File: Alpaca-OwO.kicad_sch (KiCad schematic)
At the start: 43 parts, among them J1 SWD, J2 PS360 ST1, J3 PS360 ST2, J4 Stick, J5 USB_B, J6 Pwny Pr0t, J7 I2C Quick connect, Q1 CJL3415, SW1 Reset, SW2 I2C Pullup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

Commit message: Import LCSC parts info for all components except pin headers.
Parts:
- C1, C2: value 10uF -> (none); footprint Capacitor_Tantalum_SMD:CP_EIA-3216-18_Kemet-A -> (none)
- C10, C12, C13, C14, C15, C16, C6, C7, C8, C9: value 100nF -> (none); footprint Capacitor_SMD:C_0603_1608Metric -> (none); JLC (none) -> 0603; LCSC (none) -> C1591
- C11, C5: value 1uF -> (none); footprint Capacitor_SMD:C_0603_1608Metric -> (none); JLC (none) -> 0603; LCSC (none) -> C1592
- C3, C4: value 30pF -> (none); footprint Capacitor_SMD:C_0603_1608Metric -> (none); JLC (none) -> 0603; LCSC (none) -> C713507
- F1: value 500mA -> (none); footprint Fuse:Fuse_1210_3225Metric -> (none)
- H1, H2, H3, H4: value M3 -> (none); footprint MountingHole:MountingHole_3.2mm_M3_ISO7380 -> (none)
- J1: value SWD -> (none); footprint Connector_PinHeader_2.54mm:PinHeader_1x05_P2.54mm_Vertical -> (none); JLC (none) -> Plugin,P=2.54mm
- J2: value PS360 ST1 -> (none); footprint Connector_Phoenix_MC:PhoenixContact_MC_1,5_10-G-3.5_1x10_P3.50mm_Horizontal -> (none); Comments (none) -> Use equivalent Chinese connector for JLCPCBA. Mate with Min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; JLC (none) -> P=3.5mm; LCSC (none) -> C880580
- J3: value PS360 ST2 -> (none); footprint Connector_Phoenix_MC:PhoenixContact_MC_1,5_10-G-3.5_1x10_P3.50mm_Horizontal -> (none); Comments (none) -> Use equivalent Chinese connector for JLCPCBA. Mate with Min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; JLC (none) -> P=3.5mm; LCSC (none) -> C880580
- J4: value Stick -> (none); footprint Connector_PinHeader_2.54mm:PinHeader_1x08_P2.54mm_Vertical -> (none); JLC (none) -> Plugin,P=2.54mm
- J5: value USB_B -> (none); footprint Connector_USB:USB_B_OST_USB-B1HSxx_Horizontal -> (none); JLC (none) -> Plugin; LCSC (none) -> C46392
- J6: value Pwny Pr0t -> (none); footprint Connector_PinHeader_2.54mm:PinHeader_2x08_P2.54mm_Vertical -> (none); JLC (none) -> Plugin,P=2.54mm
- J7: value I2C Quick connect -> (none); footprint Connector_JST:JST_SH_SM04B-SRSS-TB_1x04-1MP_P1.00mm_Horizontal -> (none); JLC (none) -> -; LCSC (none) -> C160404
- Q1: value CJL3415 -> (none); footprint Package_TO_SOT_SMD:SOT-23-6 -> (none)
- R1: value 10k -> (none); footprint Resistor_SMD:R_0603_1608Metric -> (none); JLC (none) -> 0603; LCSC (none) -> C98220
- R2, R5, R6, R7: value 1k -> (none); footprint Resistor_SMD:R_0603_1608Metric -> (none); JLC (none) -> 0603; LCSC (none) -> C116692
- R3, R4: value 27 -> (none); footprint Resistor_SMD:R_0603_1608Metric -> (none); JLC (none) -> 0603; LCSC (none) -> C137753
- SW1: value Reset -> (none); footprint Button_Switch_THT:SW_PUSH_6mm -> (none); JLC (none) -> Plugin; LCSC (none) -> C393938
- SW2: value I2C Pullup -> (none); footprint Button_Switch_THT:SW_DIP_SPSTx02_Slide_9.78x7.26mm_W7.62mm_P2.54mm -> (none); JLC (none) -> Plugin; LCSC (none) -> C319062
- SW3: value BootSel -> (none); footprint Button_Switch_THT:SW_PUSH_6mm -> (none); JLC (none) -> Plugin; LCSC (none) -> C393938
- U1: value AMS1117-3.3 -> (none); footprint Package_TO_SOT_SMD:SOT-223-3_TabPin2 -> (none); JLC (none) -> SOT-223; LCSC (none) -> C6186
- U2: value RP2040 -> (none); footprint private:QFN-56-1EP_7x7mm_P0.4mm_EP3.2x3.2mm_ThermalVias -> (none); JLC (none) -> QFN-56(7x7); LCSC (none) -> C2040
- U3: value W25Q32JVSS -> (none); footprint Package_SO:SOIC-8_5.23x5.23mm_P1.27mm -> (none); JLC (none) -> SOIC-8_208mil; LCSC (none) -> C82344
- Y1: value 12MHz -> (none); footprint Crystal:Crystal_HC49-4H_Vertical -> (none)

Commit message: Set screw holes as do not include
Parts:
- C1, C2: value (none) -> 10uF; footprint (none) -> Capacitor_Tantalum_SMD:CP_EIA-3216-18_Kemet-A
- C10, C12, C13, C14, C15, C16, C6, C7, C8, C9: value (none) -> 100nF; footprint (none) -> Capacitor_SMD:C_0603_1608Metric
- C11, C5: value (none) -> 1uF; footprint (none) -> Capacitor_SMD:C_0603_1608Metric
- C3, C4: value (none) -> 30pF; footprint (none) -> Capacitor_SMD:C_0603_1608Metric
- F1: value (none) -> 500mA; footprint (none) -> Fuse:Fuse_1210_3225Metric
- H1, H2, H3, H4: now left out of the parts list
- J1: value (none) -> SWD; footprint (none) -> Connector_PinHeader_2.54mm:PinHeader_1x05_P2.54mm_Vertical
- J2: value (none) -> PS360 ST1; footprint (none) -> Connector_Phoenix_MC:PhoenixContact_MC_1,5_10-G-3.5_1x10_P3.50mm_Horizontal
- J3: value (none) -> PS360 ST2; footprint (none) -> Connector_Phoenix_MC:PhoenixContact_MC_1,5_10-G-3.5_1x10_P3.50mm_Horizontal
- J4: value (none) -> Stick; footprint (none) -> Connector_PinHeader_2.54mm:PinHeader_1x08_P2.54mm_Vertical
- J5: value (none) -> USB_B; footprint (none) -> Connector_USB:USB_B_OST_USB-B1HSxx_Horizontal
- J6: value (none) -> Pwny Pr0t; footprint (none) -> Connector_PinHeader_2.54mm:PinHeader_2x08_P2.54mm_Vertical
- J7: value (none) -> I2C Quick connect; footprint (none) -> Connector_JST:JST_SH_SM04B-SRSS-TB_1x04-1MP_P1.00mm_Horizontal
- Q1: value (none) -> CJL3415; footprint (none) -> Package_TO_SOT_SMD:SOT-23-6
- R1: value (none) -> 10k; footprint (none) -> Resistor_SMD:R_0603_1608Metric
- R2, R5, R6, R7: value (none) -> 1k; footprint (none) -> Resistor_SMD:R_0603_1608Metric
- R3, R4: value (none) -> 27; footprint (none) -> Resistor_SMD:R_0603_1608Metric
- SW1: value (none) -> Reset; footprint (none) -> Button_Switch_THT:SW_PUSH_6mm
- SW2: value (none) -> I2C Pullup; footprint (none) -> Button_Switch_THT:SW_DIP_SPSTx02_Slide_9.78x7.26mm_W7.62mm_P2.54mm
- SW3: value (none) -> BootSel; footprint (none) -> Button_Switch_THT:SW_PUSH_6mm
- U1: value (none) -> AMS1117-3.3; footprint (none) -> Package_TO_SOT_SMD:SOT-223-3_TabPin2
- U2: value (none) -> RP2040; footprint (none) -> private:QFN-56-1EP_7x7mm_P0.4mm_EP3.2x3.2mm_ThermalVias
- U3: value (none) -> W25Q32JVSS; footprint (none) -> Package_SO:SOIC-8_5.23x5.23mm_P1.27mm
- Y1: value (none) -> 12MHz; footprint (none) -> Crystal:Crystal_HC49-4H_Vertical

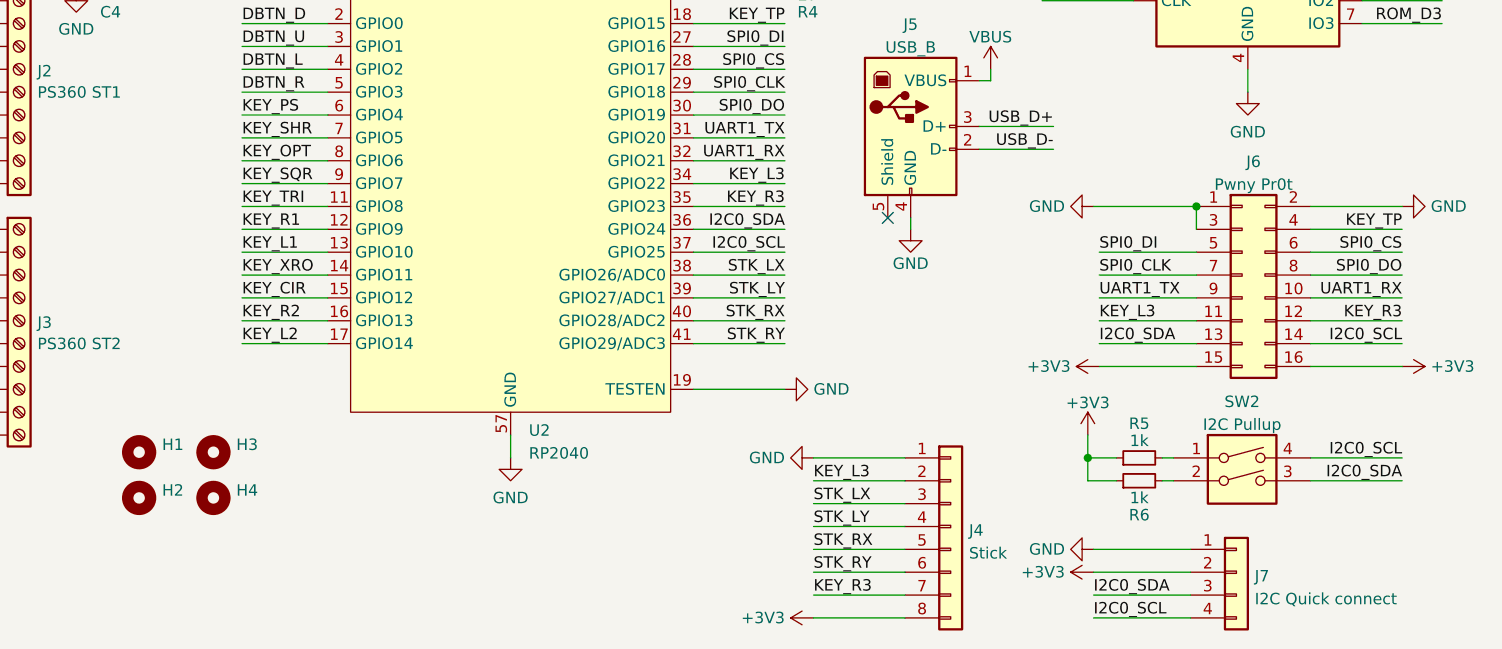
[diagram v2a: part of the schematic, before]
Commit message: v1.11
Fixed an issue where the analog stick port does not follow the Brook pinout.

No PCB routing was changed but the pin assignment for stick axis and L3/R3 buttons are now mirrored. Refer to README for the new pinout.
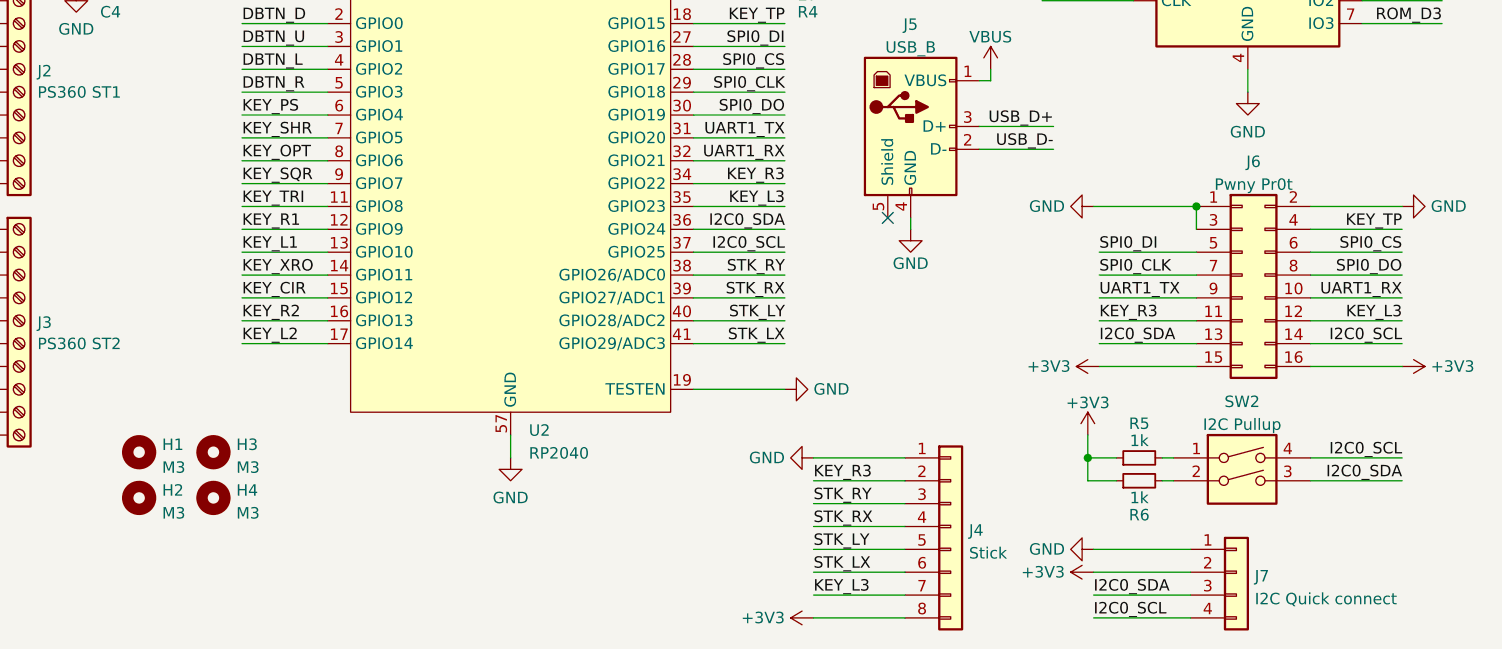
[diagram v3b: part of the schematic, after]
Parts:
- H1, H2, H3, H4: value (none) -> M3; footprint (none) -> MountingHole:MountingHole_3.2mm_M3_ISO7380
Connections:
- net KEY_L3: now also J4.7 (Pin_7), J6.12 (Pin_12), U2.35 (GPIO23); no longer J4.2 (Pin_2), J6.11 (Pin_11), U2.34 (GPIO22)
- net KEY_R3: now also J4.2 (Pin_2), J6.11 (Pin_11), U2.34 (GPIO22); no longer J4.7 (Pin_7), J6.12 (Pin_12), U2.35 (GPIO23)
- net STK_LX: now also J4.6 (Pin_6), U2.41 (GPIO29/ADC3); no longer J4.3 (Pin_3), U2.38 (GPIO26/ADC0)
- net STK_LY: now also J4.5 (Pin_5), U2.40 (GPIO28/ADC2); no longer J4.4 (Pin_4), U2.39 (GPIO27/ADC1)
- net STK_RX: now also J4.4 (Pin_4), U2.39 (GPIO27/ADC1); no longer J4.5 (Pin_5), U2.40 (GPIO28/ADC2)
- net STK_RY: now also J4.3 (Pin_3), U2.38 (GPIO26/ADC0); no longer J4.6 (Pin_6), U2.41 (GPIO29/ADC3)
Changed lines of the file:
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@@
     (title "Alpaca-OwO")
     (date "2022-02-27")
-    (rev "v1.10")
+    (rev "v1.11")
     (company "dogtopus")
   )
@@
     (effects (font (size 1.27 1.27)) (justify right bottom))
   )
-  (label "STK_LY" (at 169.545 140.97 0)
+  (label "STK_LY" (at 169.545 143.51 0)
     (effects (font (size 1.27 1.27)) (justify left bottom))
   )
@@
     (effects (font (size 1.27 1.27)) (justify left bottom))
   )
-  (label "STK_RY" (at 166.37 120.65 180)
-    (effects (font (size 1.27 1.27)) (justify right bottom))
-  )
-  (label "STK_LX" (at 166.37 113.03 180)
+  (label "STK_RY" (at 166.37 113.03 180)
+    (effects (font (size 1.27 1.27)) (justify right bottom))
+  )
+  (label "STK_LX" (at 166.37 120.65 180)
     (effects (font (size 1.27 1.27)) (justify right bottom))
   )
@@
     (effects (font (size 1.27 1.27)) (justify right bottom))
   )
-  (label "KEY_R3" (at 234.95 118.11 180)
-    (effects (font (size 1.27 1.27)) (justify right bottom))
+  (label "KEY_R3" (at 201.295 118.11 0)
+    (effects (font (size 1.27 1.27)) (justify left bottom))
   )
   (label "KEY_PS" (at 106.045 95.25 0)
@@
     (effects (font (size 1.27 1.27)) (justify right bottom))
   )
-  (label "KEY_R3" (at 166.37 105.41 180)
-    (effects (font (size 1.27 1.27)) (justify right bottom))
-  )
-  (label "KEY_L3" (at 166.37 102.87 180)
+  (label "KEY_R3" (at 166.37 102.87 180)
+    (effects (font (size 1.27 1.27)) (justify right bottom))
+  )
+  (label "KEY_L3" (at 166.37 105.41 180)
     (effects (font (size 1.27 1.27)) (justify right bottom))
   )
@@
     (effects (font (size 1.27 1.27)) (justify left bottom))
   )
-  (label "STK_RX" (at 169.545 143.51 0)
+  (label "STK_RX" (at 169.545 140.97 0)
     (effects (font (size 1.27 1.27)) (justify left bottom))
   )
@@
     (effects (font (size 1.27 1.27)) (justify left bottom))
   )
-  (label "KEY_L3" (at 169.545 135.89 0)
+  (label "KEY_L3" (at 169.545 148.59 0)
     (effects (font (size 1.27 1.27)) (justify left bottom))
   )
@@
     (effects (font (size 1.27 1.27)) (justify left bottom))
   )
-  (label "KEY_R3" (at 169.545 148.59 0)
-    (effects (font (size 1.27 1.27)) (justify left bottom))
-  )
-  (label "STK_LX" (at 169.545 138.43 0)
+  (label "KEY_R3" (at 169.545 135.89 0)
+    (effects (font (size 1.27 1.27)) (justify left bottom))
+  )
+  (label "STK_LX" (at 169.545 146.05 0)
     (effects (font (size 1.27 1.27)) (justify left bottom))
   )
@@
     (effects (font (size 1.27 1.27)) (justify left bottom))
   )
-  (label "STK_RY" (at 169.545 146.05 0)
+  (label "STK_RY" (at 169.545 138.43 0)
     (effects (font (size 1.27 1.27)) (justify left bottom))
   )
@@
     (effects (font (size 1.27 1.27)) (justify right bottom))
   )
-  (label "KEY_L3" (at 201.295 118.11 0)
-    (effects (font (size 1.27 1.27)) (justify left bottom))
+  (label "KEY_L3" (at 234.95 118.11 180)
+    (effects (font (size 1.27 1.27)) (justify right bottom))
   )
   (label "USB_D+" (at 181.61 80.01 180)
@@
     (effects (font (size 1.27 1.27)) (justify left bottom))
   )
-  (label "STK_LY" (at 166.37 115.57 180)
+  (label "STK_LY" (at 166.37 118.11 180)
     (effects (font (size 1.27 1.27)) (justify right bottom))
   )
@@
     (effects (font (size 1.27 1.27)) (justify right bottom))
   )
-  (label "STK_RX" (at 166.37 118.11 180)
+  (label "STK_RX" (at 166.37 115.57 180)
     (effects (font (size 1.27 1.27)) (justify right bottom))
   )
@@
       (effects (font (size 1.27 1.27)) (justify left))
     )
-    (property "Value" "" (id 1) (at 97.155 139.4972 0)
-      (effects (font (size 1.27 1.27)) (justify left))
-    )
-    (property "Footprint" "" (id 2) (at 94.615 137.795 0)
+    (property "Value" "M3" (id 1) (at 97.155 139.4972 0)
+      (effects (font (size 1.27 1.27)) (justify left))
+    )
+    (property "Footprint" "MountingHole:MountingHole_3.2mm_M3_ISO7380" (id 2) (at 94.615 137.795 0)
       (effects (font (size 1.27 1.27)) hide)
     )
@@
       (effects (font (size 1.27 1.27)) (justify left))
     )
-    (property "Value" "" (id 1) (at 97.155 134.4172 0)
-      (effects (font (size 1.27 1.27)) (justify left))
-    )
-    (property "Footprint" "" (id 2) (at 94.615 132.715 0)
+    (property "Value" "M3" (id 1) (at 97.155 134.4172 0)
+      (effects (font (size 1.27 1.27)) (justify left))
+    )
+    (property "Footprint" "MountingHole:MountingHole_3.2mm_M3_ISO7380" (id 2) (at 94.615 132.715 0)
       (effects (font (size 1.27 1.27)) hide)
     )
@@
       (effects (font (size 1.27 1.27)) (justify left))
     )
-    (property "Value" "" (id 1) (at 105.41 134.4172 0)
-      (effects (font (size 1.27 1.27)) (justify left))
-    )
-    (property "Footprint" "" (id 2) (at 102.87 132.715 0)
+    (property "Value" "M3" (id 1) (at 105.41 134.4172 0)
+      (effects (font (size 1.27 1.27)) (justify left))
+    )
+    (property "Footprint" "MountingHole:MountingHole_3.2mm_M3_ISO7380" (id 2) (at 102.87 132.715 0)
       (effects (font (size 1.27 1.27)) hide)
     )
@@
       (effects (font (size 1.27 1.27)) (justify left))
     )
-    (property "Value" "" (id 1) (at 105.41 139.4972 0)
-      (effects (font (size 1.27 1.27)) (justify left))
-    )
-    (property "Footprint" "" (id 2) (at 102.87 137.795 0)
-      (effects (font (size 1.27 1.27)) hide)
-    )
+    (property "Value" "M3" (id 1) (at 105.41 139.4972 0)
+      (effects (font (size 1.27 1.27)) (justify left))
+    )
+    (property "Footprint" "MountingHole:MountingHole_3.2mm_M3_ISO7380" (id 2) (at 102.87 137.795 0)
+      (effects (font (size 1.27 1.27)) hide)
+    )
